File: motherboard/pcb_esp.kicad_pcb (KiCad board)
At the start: 2 copper layers, 77 x 57 mm, 27 parts, among them J1 CONN_01X07, J3 CONN_01X17, J4 CONN_01X13, Q1 S8050, Q2 S8050, U1 LP38691, U2 ESP-12E, U3 USB

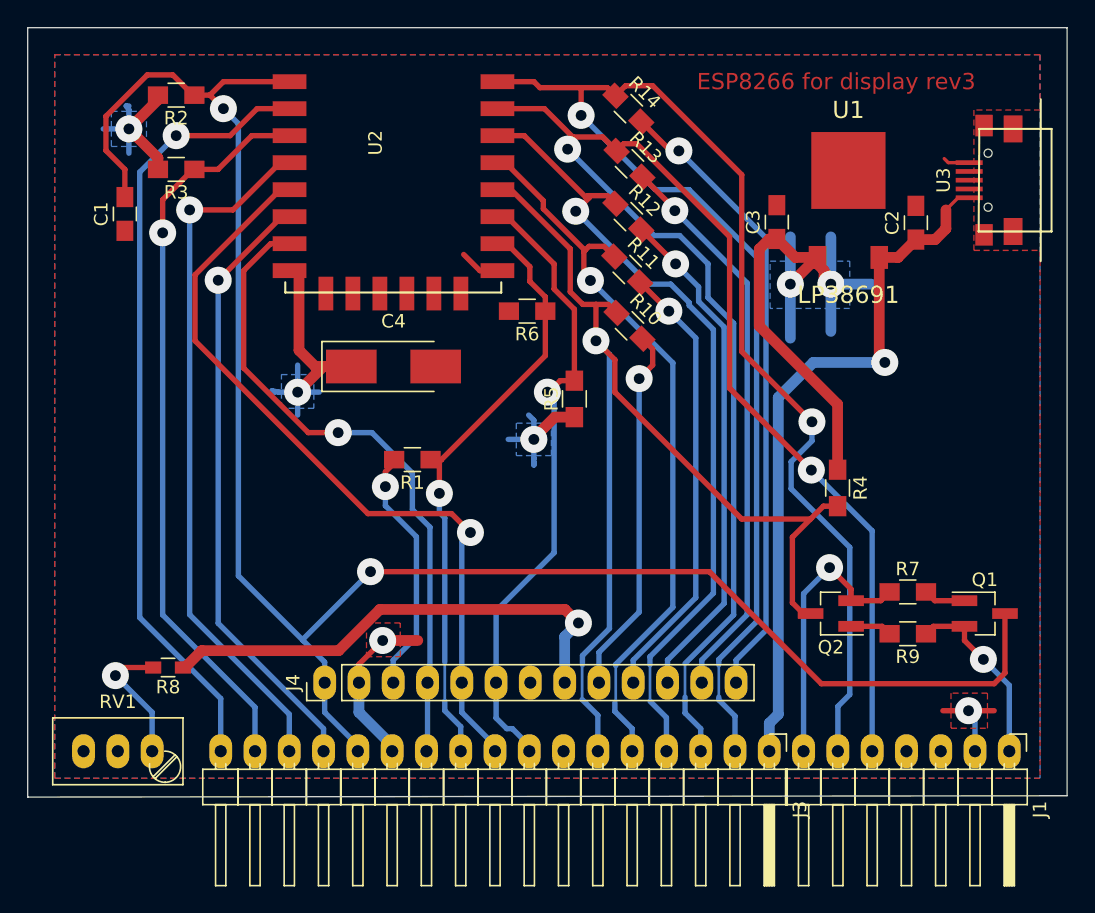
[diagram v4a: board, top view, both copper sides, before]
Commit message: Few routing tweaks following increased clearances
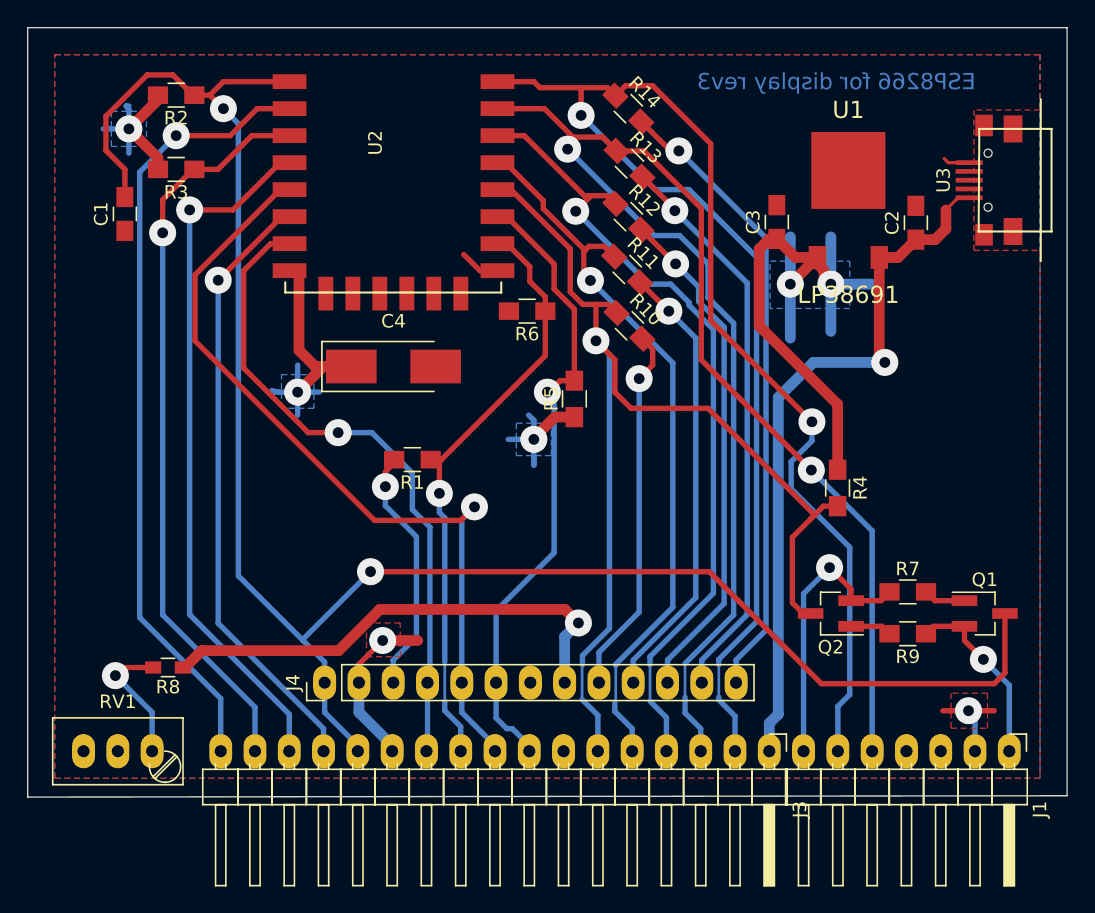
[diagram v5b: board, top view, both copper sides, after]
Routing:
- net /sck_gpio14: track 59.0 -> 61.3 mm
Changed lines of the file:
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@@
-(kicad_pcb (version 20170123) (host pcbnew "(2017-07-25 revision 161045f17)-master")
+(kicad_pcb (version 20170123) (host pcbnew "(2017-08-04 revision 7bf9f8e1c)-master")
   (general
     (thickness 1.6)
     (drawings 6)
-    (tracks 411)
+    (tracks 413)
     (zones 0)
     (modules 27)
@@
     )
   )
-  (gr_text "ESP8266 for display rev3" (at 107.9 52) (layer F.Cu)
-    (effects (font (size 1.2 1.2) (thickness 0.25)))
+  (gr_text "ESP8266 for display rev3" (at 107.9 52) (layer B.Cu)
+    (effects (font (size 1.2 1.2) (thickness 0.25)) (justify mirror))
   )
   (gr_line (start 124 98) (end 48 98) (layer Dwgs.User) (width 0.2))
@@
   (segment (start 117.4 92.35) (end 115.1 92.35) (width 0.4) (layer F.Cu) (net 4) (status 30))
   (segment (start 115.1 92.35) (end 114.55 92.9) (width 0.4) (layer F.Cu) (net 4) (status 30))
+  (segment (start 97.904989 72.623468) (end 105.055 79.773479) (width 0.4) (layer F.Cu) (net 6))
+  (segment (start 97.904989 61.387882) (end 97.904989 72.623468) (width 0.4) (layer F.Cu) (net 6))
+  (segment (start 93.648299 57.131192) (end 97.904989 61.387882) (width 0.4) (layer F.Cu) (net 6))
+  (segment (start 91.631192 57.131192) (end 93.648299 57.131192) (width 0.4) (layer F.Cu) (net 6))
+  (segment (start 105.055 79.773479) (end 106.054999 80.773478) (width 0.4) (layer F.Cu) (net 6))
   (segment (start 88 57) (end 88 56.487396) (width 0.4) (layer F.Cu) (net 6))
   (segment (start 88 56.487396) (end 88.387396 56.1) (width 0.4) (layer F.Cu) (net 6))
@@
   (segment (start 90.6 56.1) (end 91.631192 57.131192) (width 0.4) (layer F.Cu) (net 6) (status 20))
   (segment (start 86.287396 54) (end 88.387396 56.1) (width 0.4) (layer F.Cu) (net 6))
-  (segment (start 91.631192 57.131192) (end 92.161521 56.600863) (width 0.4) (layer F.Cu) (net 6) (status 10))
-  (segment (start 92.161521 56.600863) (end 93.11797 56.600863) (width 0.4) (layer F.Cu) (net 6))
-  (segment (start 93.11797 56.600863) (end 100 63.482893) (width 0.4) (layer F.Cu) (net 6))
-  (segment (start 100 74.718479) (end 106.054999 80.773478) (width 0.4) (layer F.Cu) (net 6))
-  (segment (start 100 63.482893) (end 100 74.718479) (width 0.4) (layer F.Cu) (net 6))
   (segment (start 110.56 85.278479) (end 106.054999 80.773478) (width 0.4) (layer B.Cu) (net 6))
   (segment (start 110.56 101.6) (end 110.56 85.278479) (width 0.4) (layer B.Cu) (net 6) (status 10))
@@
   (segment (start 97.86 101.6) (end 97.86 99.93) (width 0.4) (layer B.Cu) (net 6) (status 10))
   (segment (start 97.86 99.93) (end 96.7 98.77) (width 0.4) (layer B.Cu) (net 6))
-  (segment (start 106.1 77.2) (end 100.9 72) (width 0.4) (layer F.Cu) (net 7))
-  (segment (start 100.9 72) (end 100.9 58.9) (width 0.4) (layer F.Cu) (net 7))
+  (segment (start 92.290812 52.3) (end 91.545406 53.045406) (width 0.4) (layer F.Cu) (net 7))
+  (segment (start 106.1 77.2) (end 98.6 69.7) (width 0.4) (layer F.Cu) (net 7))
   (segment (start 94.3 52.3) (end 92.290812 52.3) (width 0.4) (layer F.Cu) (net 7))
-  (segment (start 100.9 58.9) (end 94.3 52.3) (width 0.4) (layer F.Cu) (net 7))
-  (segment (start 92.290812 52.3) (end 91.545406 53.045406) (width 0.4) (layer F.Cu) (net 7) (status 20))
+  (segment (start 98.6 69.7) (end 98.6 56.6) (width 0.4) (layer F.Cu) (net 7))
+  (segment (start 98.6 56.6) (end 94.3 52.3) (width 0.4) (layer F.Cu) (net 7))
   (segment (start 85.944366 52.444366) (end 89 52.444366) (width 0.4) (layer F.Cu) (net 7))
   (segment (start 89 52.444366) (end 90.944366 52.444366) (width 0.4) (layer F.Cu) (net 7))
@@
   (segment (start 63.208998 61.5) (end 60 61.5) (width 0.4) (layer F.Cu) (net 11))
   (via (at 60 61.5) (size 2) (drill 0.8) (layers F.Cu B.Cu) (net 11))
-  (segment (start 80.8 85.4) (end 80.16 86.04) (width 0.4) (layer B.Cu) (net 12))
-  (segment (start 80.16 86.04) (end 80.16 96.52) (width 0.4) (layer B.Cu) (net 12) (status 20))
-  (segment (start 73.2 84) (end 79.4 84) (width 0.4) (layer F.Cu) (net 12))
-  (segment (start 79.4 84) (end 80.8 85.4) (width 0.4) (layer F.Cu) (net 12))
-  (via (at 80.8 85.4) (size 2) (drill 0.8) (layers F.Cu B.Cu) (net 12))
-  (segment (start 60.4 71.2) (end 73.2 84) (width 0.4) (layer F.Cu) (net 12))
+  (segment (start 80.100001 84.499999) (end 81.1 83.5) (width 0.4) (layer F.Cu) (net 12))
+  (segment (start 73.699999 84.499999) (end 80.100001 84.499999) (width 0.4) (layer F.Cu) (net 12))
   (segment (start 60.4 66.308998) (end 60.4 71.2) (width 0.4) (layer F.Cu) (net 12))
-  (segment (start 68.1 60) (end 66.708998 60) (width 0.4) (layer F.Cu) (net 12) (status 30))
-  (segment (start 66.708998 60) (end 60.4 66.308998) (width 0.4) (layer F.Cu) (net 12) (status 10))
+  (segment (start 66.708998 60) (end 60.4 66.308998) (width 0.4) (layer F.Cu) (net 12))
+  (segment (start 60.4 71.2) (end 73.699999 84.499999) (width 0.4) (layer F.Cu) (net 12))
+  (segment (start 68.1 60) (end 66.708998 60) (width 0.4) (layer F.Cu) (net 12))
+  (segment (start 80.16 84.44) (end 81.1 83.5) (width 0.4) (layer B.Cu) (net 12))
+  (segment (start 80.16 96.52) (end 80.16 84.44) (width 0.4) (layer B.Cu) (net 12))
+  (via (at 81.1 83.5) (size 2) (drill 0.8) (layers F.Cu B.Cu) (net 12))
   (segment (start 80.16 96.52) (end 80.16 98.72) (width 0.4) (layer B.Cu) (net 12) (status 10))
   (segment (start 80.16 98.72) (end 82.62 101.18) (width 0.4) (layer B.Cu) (net 12) (status 20))
@@
   (segment (start 92.78 101.6) (end 92.78 99.93) (width 0.4) (layer B.Cu) (net 16) (status 10))
   (segment (start 92.78 99.93) (end 91.5 98.65) (width 0.4) (layer B.Cu) (net 16))
+  (segment (start 92.7 76.2) (end 91.5 75) (width 0.4) (layer F.Cu) (net 17))
+  (segment (start 106 84.4) (end 106.3 84.1) (width 0.4) (layer F.Cu) (net 17))
+  (segment (start 106.3 84.1) (end 106.95 83.45) (width 0.4) (layer F.Cu) (net 17))
+  (segment (start 92.7 76.2) (end 98.4 76.2) (width 0.4) (layer F.Cu) (net 17))
+  (segment (start 98.4 76.2) (end 106.3 84.1) (width 0.4) (layer F.Cu) (net 17))
   (segment (start 89.123894 68.5) (end 90.1 68.5) (width 0.4) (layer F.Cu) (net 17))
   (segment (start 90.1 68.5) (end 91 68.5) (width 0.4) (layer F.Cu) (net 17))
@@
   (segment (start 91.5 75) (end 91.5 72.6) (width 0.4) (layer F.Cu) (net 17))
   (segment (start 91.5 72.6) (end 90.1 71.2) (width 0.4) (layer F.Cu) (net 17))
-  (segment (start 100.9 84.4) (end 91.5 75) (width 0.4) (layer F.Cu) (net 17))
-  (segment (start 106 84.4) (end 100.9 84.4) (width 0.4) (layer F.Cu) (net 17))
-  (segment (start 106 84.4) (end 106.95 83.45) (width 0.4) (layer F.Cu) (net 17))
   (segment (start 106.95 83.45) (end 108 83.45) (width 0.4) (layer F.Cu) (net 17) (status 20))
   (segment (start 88.195011 64.390508) (end 88.195011 67.571117) (width 0.4) (layer F.Cu) (net 17))
